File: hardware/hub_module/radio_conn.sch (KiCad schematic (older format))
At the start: 0 parts

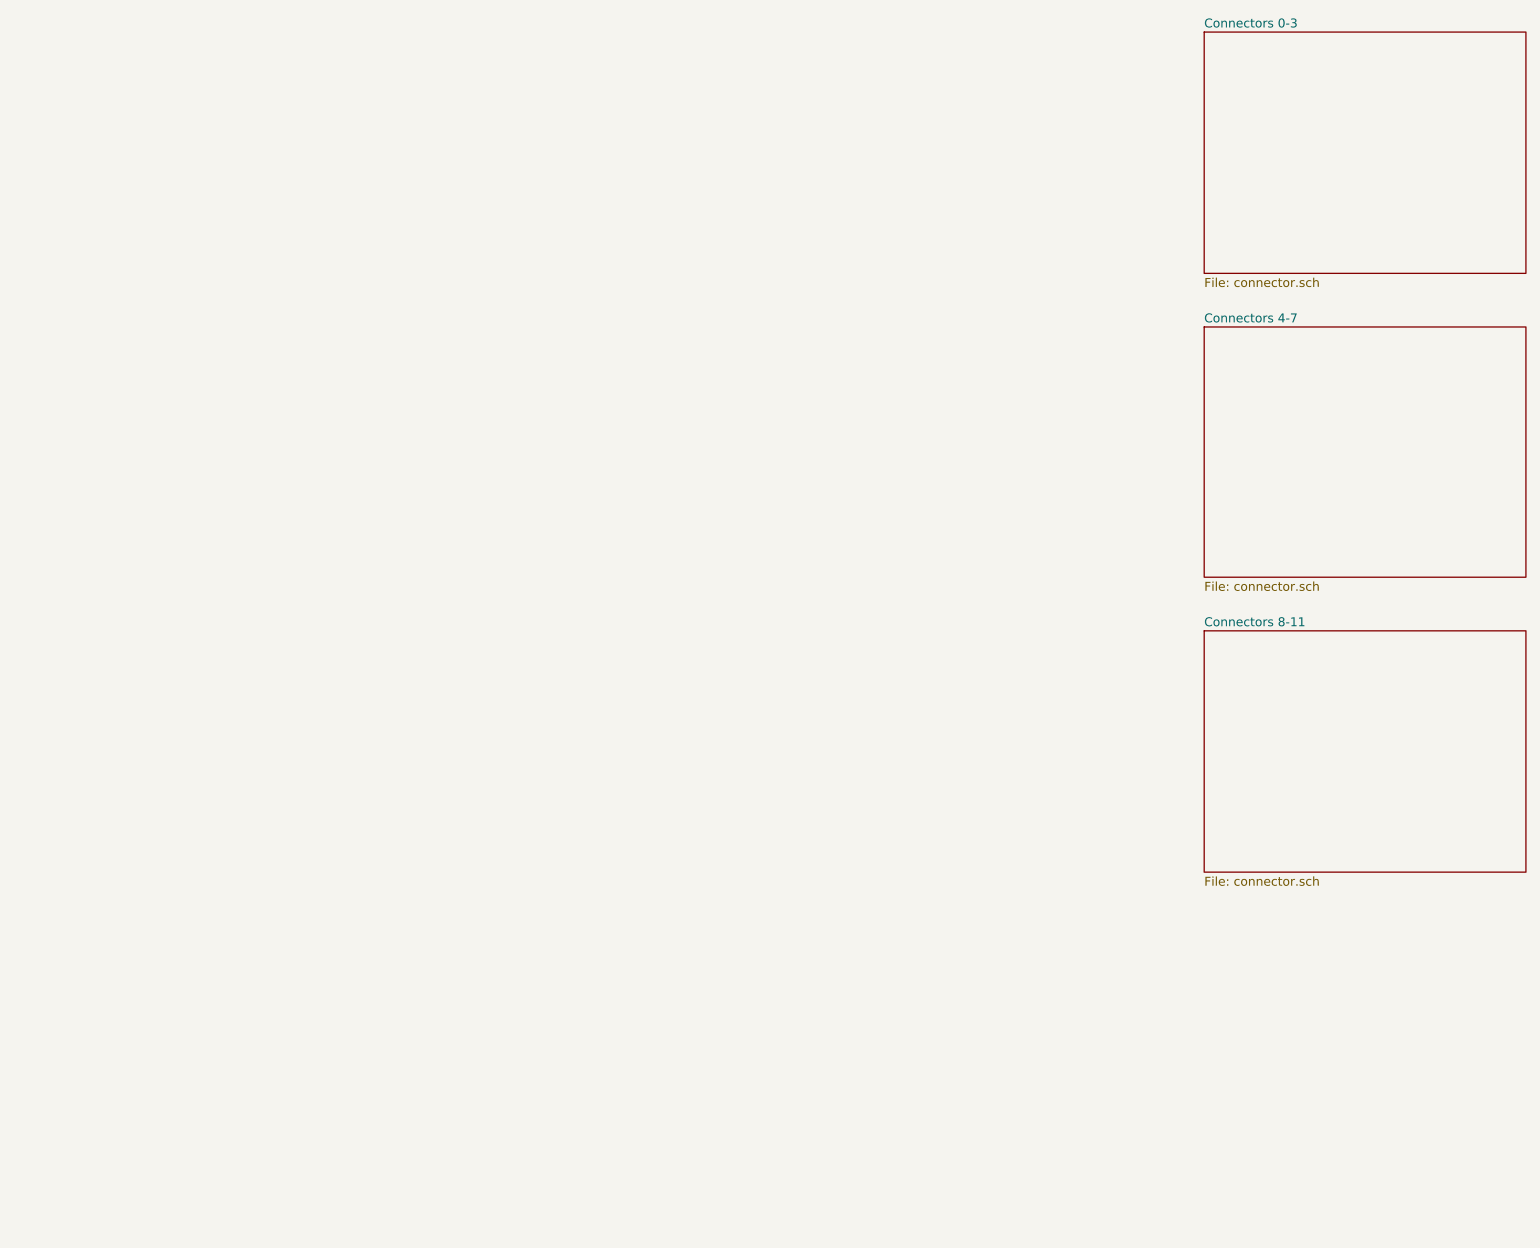
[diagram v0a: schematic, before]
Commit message: busses added
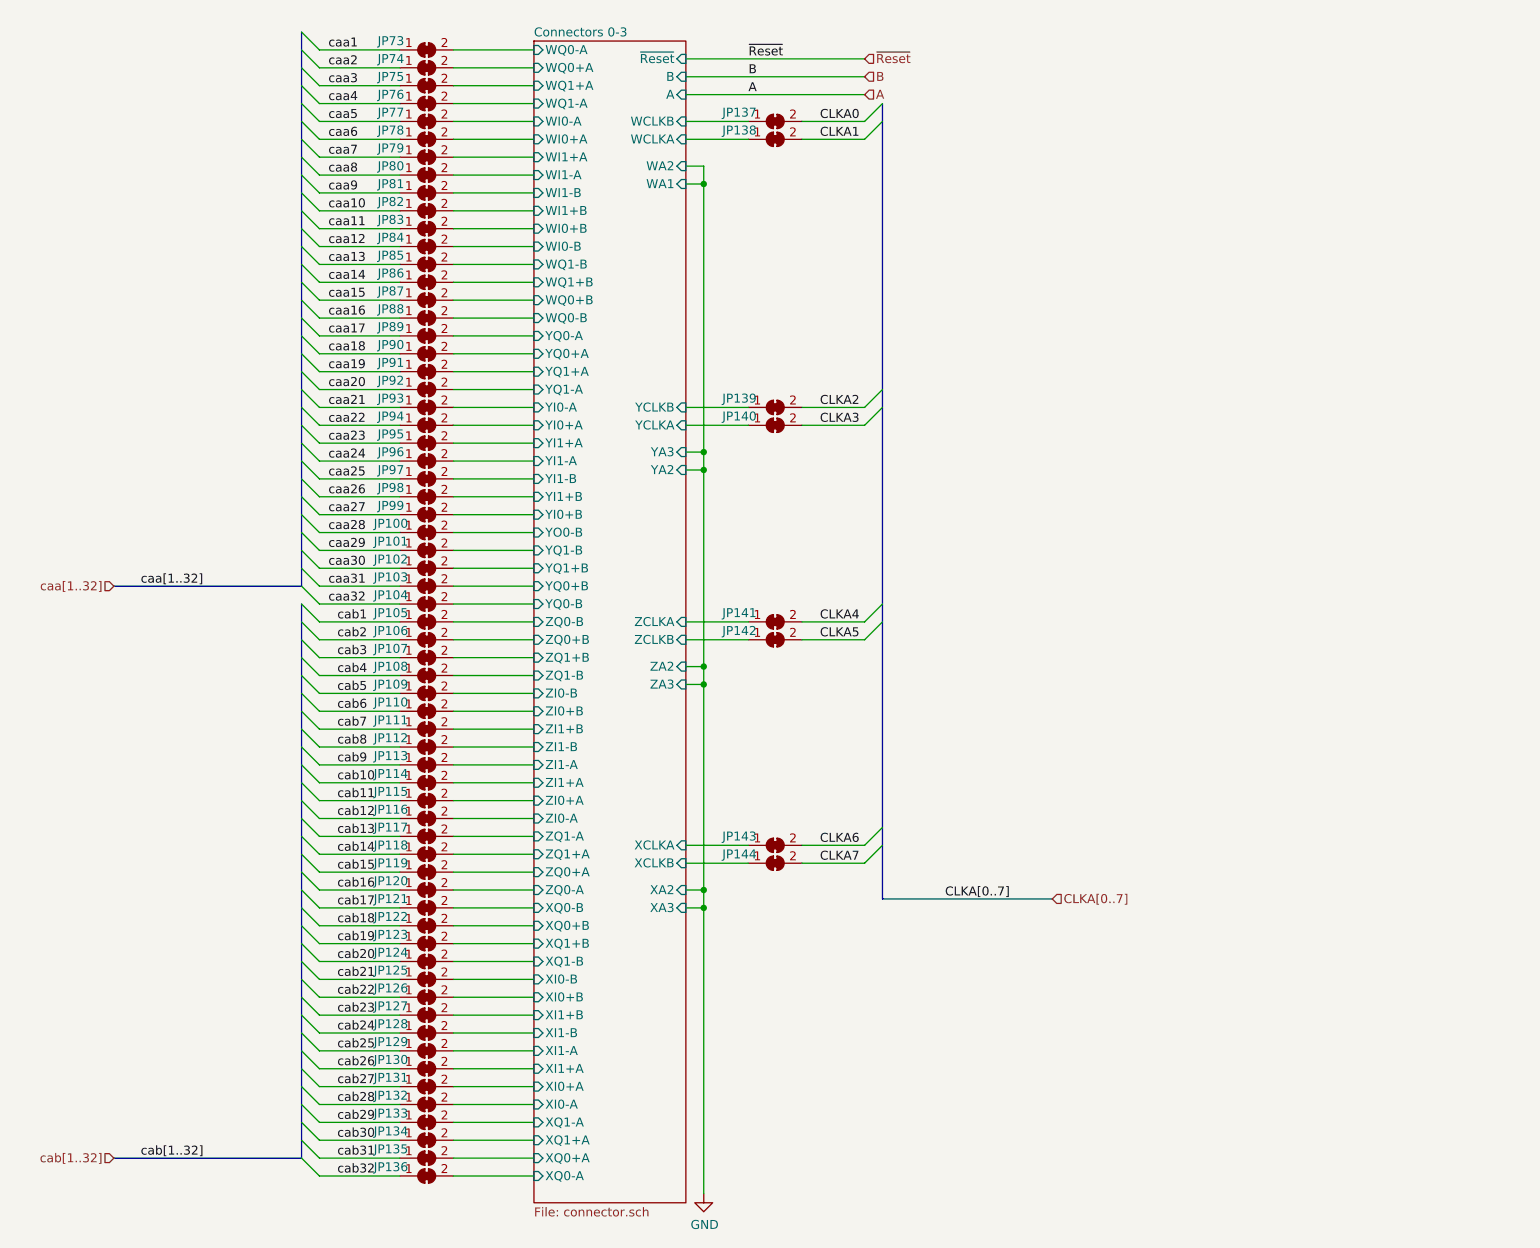
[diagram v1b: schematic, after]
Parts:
- added JP100, JP101, JP102, JP103, JP104, JP105, JP106, JP107, JP108, JP109, JP110, JP111, JP112, JP113, JP114, JP115, JP116, JP117, JP118, JP119, JP120, JP121, JP122, JP123, JP124, JP125, JP126, JP127, JP128, JP129, JP130, JP131, JP132, JP133, JP134, JP135, JP136, JP137, JP138, JP139, JP140, JP141, JP142, JP143, JP144, JP73, JP74, JP75, JP76, JP77, JP78, JP79, JP80, JP81, JP82, JP83, JP84, JP85, JP86, JP87, JP88, JP89, JP90, JP91, JP92, JP93, JP94, JP95, JP96, JP97, JP98, JP99: SolderJumper_2_Bridged, Jumper:SolderJumper-2_P1.3mm_Bridged2Bar_Pad1.0x1.5mm, symbol Jumper:SolderJumper_2_Bridged
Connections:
- new net CLKA0: JP137.2 (B)
- new net CLKA1: JP138.2 (B)
- new net CLKA2: JP139.2 (B)
- new net CLKA3: JP140.2 (B)
- new net CLKA4: JP141.2 (B)
- new net CLKA5: JP142.2 (B)
- new net CLKA6: JP143.2 (B)
- new net CLKA7: JP144.2 (B)
- new net Connectors 0-3/WCLKA: JP138.1 (A)
- new net Connectors 0-3/WCLKB: JP137.1 (A)
- new net Connectors 0-3/WI0+A: JP78.2 (B)
- new net Connectors 0-3/WI0+B: JP83.2 (B)
- new net Connectors 0-3/WI0-A: JP77.2 (B)
- new net Connectors 0-3/WI0-B: JP84.2 (B)
- new net Connectors 0-3/WI1+A: JP79.2 (B)
- new net Connectors 0-3/WI1+B: JP82.2 (B)
- new net Connectors 0-3/WI1-A: JP80.2 (B)
- new net Connectors 0-3/WI1-B: JP81.2 (B)
- new net Connectors 0-3/WQ0+A: JP74.2 (B)
- new net Connectors 0-3/WQ0+B: JP87.2 (B)
- new net Connectors 0-3/WQ0-A: JP73.2 (B)
- new net Connectors 0-3/WQ0-B: JP88.2 (B)
- new net Connectors 0-3/WQ1+A: JP75.2 (B)
- new net Connectors 0-3/WQ1+B: JP86.2 (B)
- new net Connectors 0-3/WQ1-A: JP76.2 (B)
- new net Connectors 0-3/WQ1-B: JP85.2 (B)
- new net Connectors 0-3/XCLKA: JP143.1 (A)
- new net Connectors 0-3/XCLKB: JP144.1 (A)
- new net Connectors 0-3/XI0+A: JP131.2 (B)
- new net Connectors 0-3/XI0+B: JP126.2 (B)
- new net Connectors 0-3/XI0-A: JP132.2 (B)
- new net Connectors 0-3/XI0-B: JP125.2 (B)
- new net Connectors 0-3/XI1+A: JP130.2 (B)
- new net Connectors 0-3/XI1+B: JP127.2 (B)
- new net Connectors 0-3/XI1-A: JP129.2 (B)
- new net Connectors 0-3/XI1-B: JP128.2 (B)
- new net Connectors 0-3/XQ0+A: JP135.2 (B)
- new net Connectors 0-3/XQ0+B: JP122.2 (B)
- new net Connectors 0-3/XQ0-A: JP136.2 (B)
- new net Connectors 0-3/XQ0-B: JP121.2 (B)
- new net Connectors 0-3/XQ1+A: JP134.2 (B)
- new net Connectors 0-3/XQ1+B: JP123.2 (B)
- new net Connectors 0-3/XQ1-A: JP133.2 (B)
- new net Connectors 0-3/XQ1-B: JP124.2 (B)
- new net Connectors 0-3/YCLKA: JP140.1 (A)
- new net Connectors 0-3/YCLKB: JP139.1 (A)
- new net Connectors 0-3/YI0+A: JP94.2 (B)
- new net Connectors 0-3/YI0+B: JP99.2 (B)
- new net Connectors 0-3/YI0-A: JP93.2 (B)
- new net Connectors 0-3/YI1+A: JP95.2 (B)
- new net Connectors 0-3/YI1+B: JP98.2 (B)
- new net Connectors 0-3/YI1-A: JP96.2 (B)
- new net Connectors 0-3/YI1-B: JP97.2 (B)
- new net Connectors 0-3/YO0-B: JP100.2 (B)
- new net Connectors 0-3/YQ0+A: JP90.2 (B)
- new net Connectors 0-3/YQ0+B: JP103.2 (B)
- new net Connectors 0-3/YQ0-A: JP89.2 (B)
- new net Connectors 0-3/YQ0-B: JP104.2 (B)
- new net Connectors 0-3/YQ1+A: JP91.2 (B)
- new net Connectors 0-3/YQ1+B: JP102.2 (B)
- new net Connectors 0-3/YQ1-A: JP92.2 (B)
- new net Connectors 0-3/YQ1-B: JP101.2 (B)
- new net Connectors 0-3/ZCLKA: JP141.1 (A)
- new net Connectors 0-3/ZCLKB: JP142.1 (A)
- new net Connectors 0-3/ZI0+A: JP115.2 (B)
- new net Connectors 0-3/ZI0+B: JP110.2 (B)
- new net Connectors 0-3/ZI0-A: JP116.2 (B)
- new net Connectors 0-3/ZI0-B: JP109.2 (B)
- new net Connectors 0-3/ZI1+A: JP114.2 (B)
- new net Connectors 0-3/ZI1+B: JP111.2 (B)
- new net Connectors 0-3/ZI1-A: JP113.2 (B)
- new net Connectors 0-3/ZI1-B: JP112.2 (B)
- new net Connectors 0-3/ZQ0+A: JP119.2 (B)
- new net Connectors 0-3/ZQ0+B: JP106.2 (B)
- new net Connectors 0-3/ZQ0-A: JP120.2 (B)
- new net Connectors 0-3/ZQ0-B: JP105.2 (B)
- new net Connectors 0-3/ZQ1+A: JP118.2 (B)
- new net Connectors 0-3/ZQ1+B: JP107.2 (B)
- new net Connectors 0-3/ZQ1-A: JP117.2 (B)
- new net Connectors 0-3/ZQ1-B: JP108.2 (B)
- new net caa1: JP73.1 (A)
- new net caa10: JP82.1 (A)
- new net caa11: JP83.1 (A)
- new net caa12: JP84.1 (A)
- new net caa13: JP85.1 (A)
- new net caa14: JP86.1 (A)
- new net caa15: JP87.1 (A)
- new net caa16: JP88.1 (A)
- new net caa17: JP89.1 (A)
- new net caa18: JP90.1 (A)
- new net caa19: JP91.1 (A)
- new net caa2: JP74.1 (A)
- new net caa20: JP92.1 (A)
- new net caa21: JP93.1 (A)
- new net caa22: JP94.1 (A)
- new net caa23: JP95.1 (A)
- new net caa24: JP96.1 (A)
- new net caa25: JP97.1 (A)
- new net caa26: JP98.1 (A)
- new net caa27: JP99.1 (A)
- new net caa28: JP100.1 (A)
- new net caa29: JP101.1 (A)
- new net caa3: JP75.1 (A)
- new net caa30: JP102.1 (A)
- new net caa31: JP103.1 (A)
- new net caa32: JP104.1 (A)
- new net caa4: JP76.1 (A)
- new net caa5: JP77.1 (A)
- new net caa6: JP78.1 (A)
- new net caa7: JP79.1 (A)
- new net caa8: JP80.1 (A)
- new net caa9: JP81.1 (A)
- new net cab1: JP105.1 (A)
- new net cab10: JP114.1 (A)
- new net cab11: JP115.1 (A)
- new net cab12: JP116.1 (A)
- new net cab13: JP117.1 (A)
- new net cab14: JP118.1 (A)
- new net cab15: JP119.1 (A)
- new net cab16: JP120.1 (A)
- new net cab17: JP121.1 (A)
- new net cab18: JP122.1 (A)
- new net cab19: JP123.1 (A)
- new net cab2: JP106.1 (A)
- new net cab20: JP124.1 (A)
- new net cab21: JP125.1 (A)
- new net cab22: JP126.1 (A)
- new net cab23: JP127.1 (A)
- new net cab24: JP128.1 (A)
- new net cab25: JP129.1 (A)
- new net cab26: JP130.1 (A)
- new net cab27: JP131.1 (A)
- new net cab28: JP132.1 (A)
- new net cab29: JP133.1 (A)
- new net cab3: JP107.1 (A)
- new net cab30: JP134.1 (A)
- new net cab31: JP135.1 (A)
- new net cab32: JP136.1 (A)
- new net cab4: JP108.1 (A)
- new net cab5: JP109.1 (A)
- new net cab6: JP110.1 (A)
- new net cab7: JP111.1 (A)
- new net cab8: JP112.1 (A)
- new net cab9: JP113.1 (A)
